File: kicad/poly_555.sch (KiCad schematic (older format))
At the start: 32 parts, among them U1 LM386

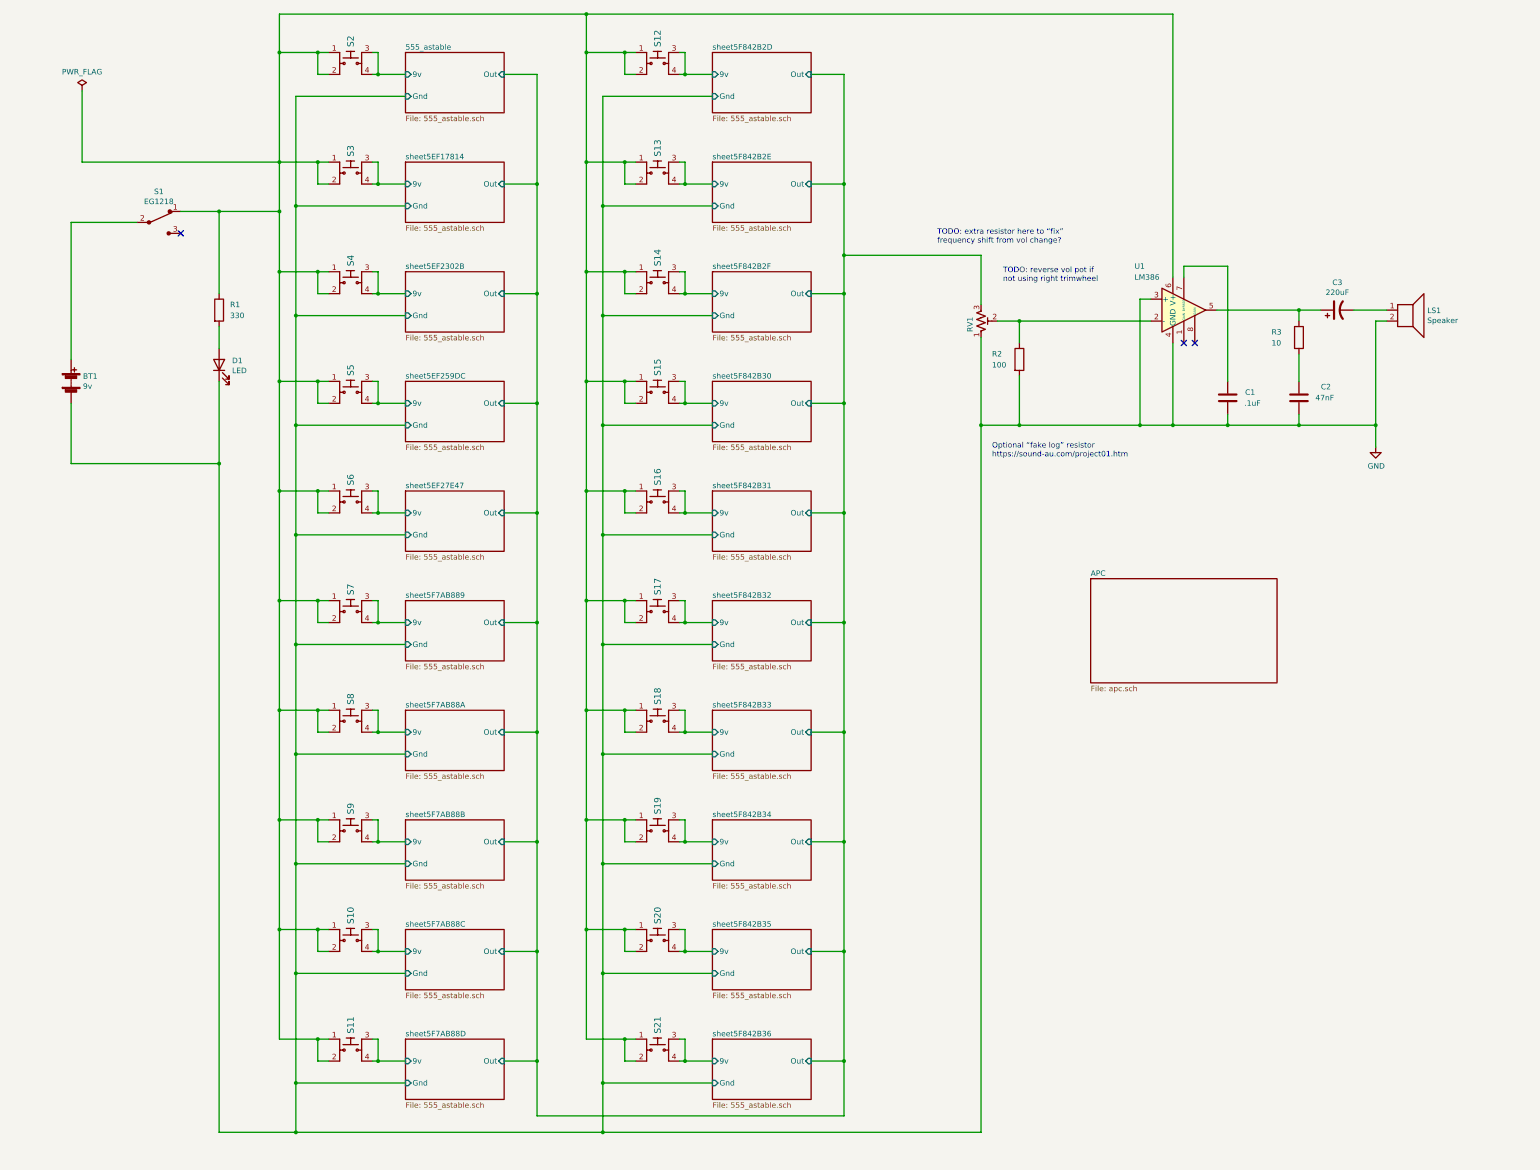
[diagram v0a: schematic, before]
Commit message: PCB revisions:
* Fix APC ground error
* Add voltage regulator to POLY_555
* Ditch hitch
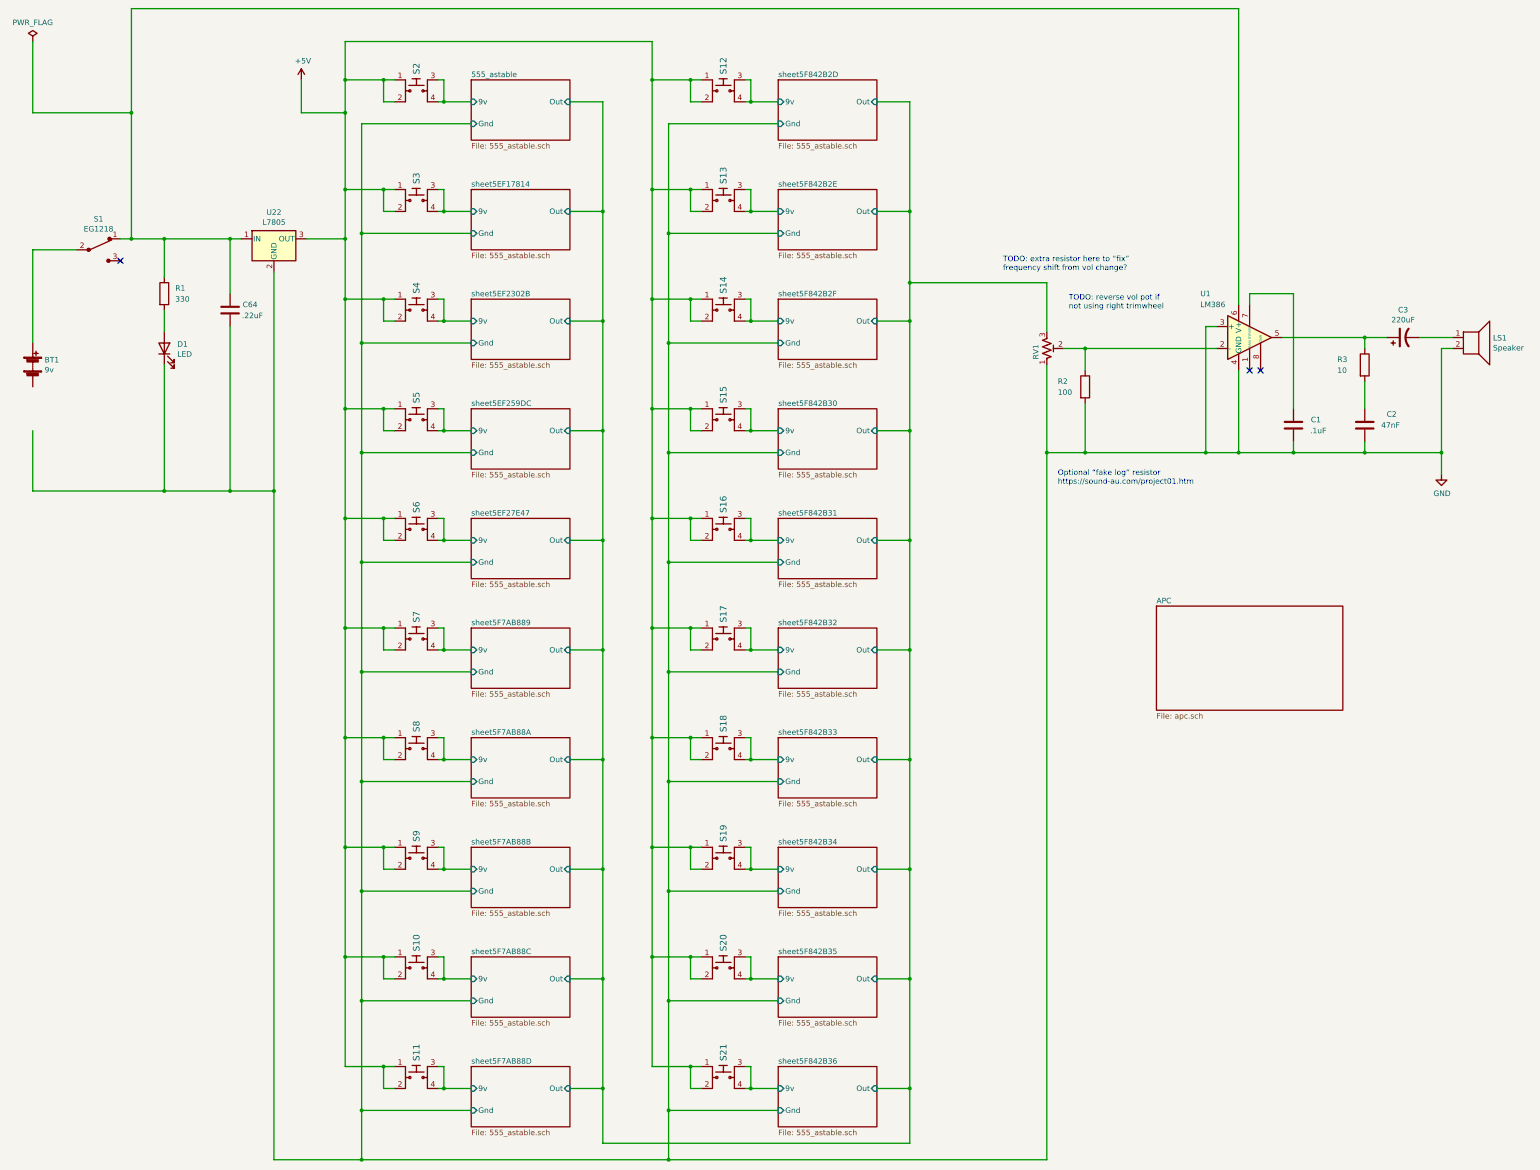
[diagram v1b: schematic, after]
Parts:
- added C64: .22uF, Capacitor_THT:C_Disc_D5.0mm_W2.5mm_P5.00mm, symbol Device:C
- added U22: L7805, Package_TO_SOT_THT:TO-220F-3_Horizontal_TabDown, symbol Regulator_Linear:L7805
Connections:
- net GND: now also C64.1, U22.2 (GND); no longer BT1.2 (-)
- net +5V: now reaches S10.1, S10.2, S11.1, S11.2, S12.1, S12.2, S13.1, S13.2, S14.1, S14.2, S15.1, S15.2, S16.1, S16.2, S17.1, S17.2, S18.1, S18.2, S19.1, S19.2, S2.1, S2.2, S20.1, S20.2, S21.1, S21.2, S3.1, S3.2, S4.1, S4.2, S5.1, S5.2, S6.1, S6.2, S7.1, S7.2, S8.1, S8.2, S9.1, S9.2
- net +5V: now also U22.3 (OUT); no longer R1.1, S1.1, U1.6 (V+)
- new net: C64.2, R1.1, S1.1, U1.6 (V+), U22.1 (IN)
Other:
- moved on the sheet: BT1, C1, C2, C3, D1, LS1, R1, R2, R3, RV1, S1, S10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

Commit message: Reorder components left to right
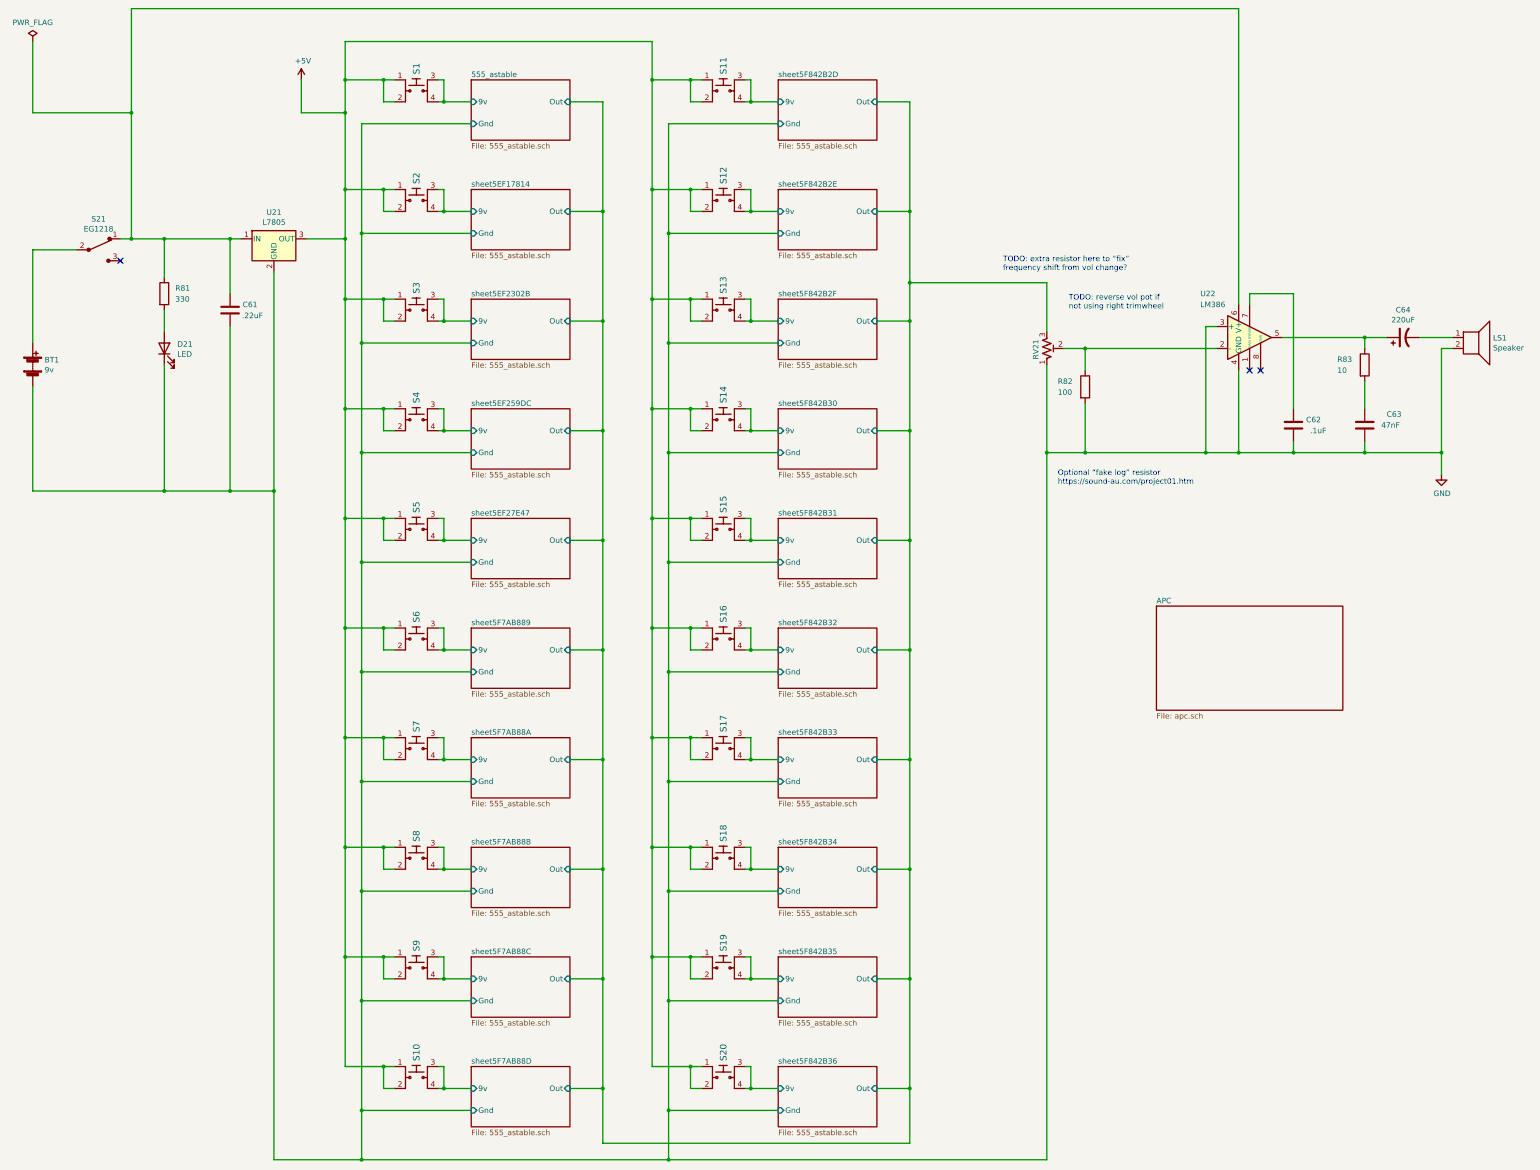
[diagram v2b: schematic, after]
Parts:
- removed C1: .1uF, Capacitor_THT:C_Disc_D5.0mm_W2.5mm_P5.00mm, symbol Device:C
- removed C2: 47nF, Capacitor_THT:C_Disc_D5.0mm_W2.5mm_P5.00mm, symbol Device:C
- removed C3: 220uF, Capacitor_THT:CP_Radial_D8.0mm_P3.50mm, symbol Device:CP1
- removed C64: .22uF, Capacitor_THT:C_Disc_D5.0mm_W2.5mm_P5.00mm, symbol Device:C
- removed D1: LED, LED_THT:LED_D5.0mm, symbol Device:LED
- removed R1: 330, Resistor_THT:R_Axial_DIN0207_L6.3mm_D2.5mm_P2.54mm_Vertical, symbol Device:R
- removed R2: 100, Resistor_THT:R_Axial_DIN0207_L6.3mm_D2.5mm_P10.16mm_Horizontal, symbol Device:R
- removed R3: 10, Resistor_THT:R_Axial_DIN0207_L6.3mm_D2.5mm_P2.54mm_Vertical, symbol Device:R
- removed RV1: R_POT_TRIM_US, Potentiometer_THT:Potentiometer_Piher_PT-6-V_Vertical, symbol Device:R_POT_TRIM_US
- removed S1: EG1218, Button_Switch_THT:SW_Slide_1P2T_CK_OS102011MS2Q, symbol dk_Slide-Switches:EG1218
- removed U1: LM386, Package_DIP:DIP-8_W7.62mm, symbol Amplifier_Audio:LM386
- removed U22: L7805, Package_TO_SOT_THT:TO-220F-3_Horizontal_TabDown, symbol Regulator_Linear:L7805
- added C61: .22uF, Capacitor_THT:C_Disc_D5.0mm_W2.5mm_P5.00mm, symbol Device:C
- added C62: .1uF, Capacitor_THT:C_Disc_D5.0mm_W2.5mm_P5.00mm, symbol Device:C
- added C63: 47nF, Capacitor_THT:C_Disc_D5.0mm_W2.5mm_P5.00mm, symbol Device:C
- added C64: 220uF, Capacitor_THT:CP_Radial_D8.0mm_P3.50mm, symbol Device:CP1
- added D21: LED, LED_THT:LED_D5.0mm, symbol Device:LED
- added R81: 330, Resistor_THT:R_Axial_DIN0207_L6.3mm_D2.5mm_P2.54mm_Vertical, symbol Device:R
- added R82: 100, Resistor_THT:R_Axial_DIN0207_L6.3mm_D2.5mm_P10.16mm_Horizontal, symbol Device:R
- added R83: 10, Resistor_THT:R_Axial_DIN0207_L6.3mm_D2.5mm_P2.54mm_Vertical, symbol Device:R
- added RV21: R_POT_TRIM_US, Potentiometer_THT:Potentiometer_Piher_PT-6-V_Vertical, symbol Device:R_POT_TRIM_US
- added S21: EG1218, Button_Switch_THT:SW_Slide_1P2T_CK_OS102011MS2Q, symbol dk_Slide-Switches:EG1218
- added U21: L7805, Package_TO_SOT_THT:TO-220F-3_Horizontal_TabDown, symbol Regulator_Linear:L7805
- added U22: LM386, Package_DIP:DIP-8_W7.62mm, symbol Amplifier_Audio:LM386
- renumbered S2 to S1, S11 to S10, S12 to S11, S13 to S12, S14 to S13, S15 to S14, S16 to S15, S17 to S16, S18 to S17, S19 to S18, S20 to S19, S3 to S2, S21 to S20, S4 to S3, S5 to S4, S6 to S5, S7 to S6, S8 to S7, S9 to S8, S10 to S9
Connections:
- net +5V: now also U21.3 (OUT)
- net 555_astable/Out: now also RV21.3
- net GND: now also BT1.2 (-), C61.1, C62.1, C63.2, D21.1 (K), R82.2, RV21.1, U21.2 (GND), U22.3 (+), U22.4 (GND)
- net at BT1.1 (+): now also S21.2
- net at LS1.1: now also C64.2
- new net: D21.2 (A), R81.2
- new net: C61.2, R81.1, S21.1, U21.1 (IN), U22.6 (V+)
- new net: R82.1, RV21.2, U22.2 (-)
- new net: C63.1, R83.2
- new net: C64.1, R83.1, U22.5
- new net: C62.2, U22.7 (BYPASS)
